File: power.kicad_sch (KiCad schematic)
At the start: 89 parts, among them Q1 PJE138K, Q2 PJE138K, Q3 SSM3J332R, Q4 PJE138K, Q5 SSM3J332R, Q6 PJE138K, Q7 SSM3J332R, U1 TLV70018_SC70, U4 TPS65150_HTSSOP, U5 MPQ7235GQBE, U6 TLV76701_WSON

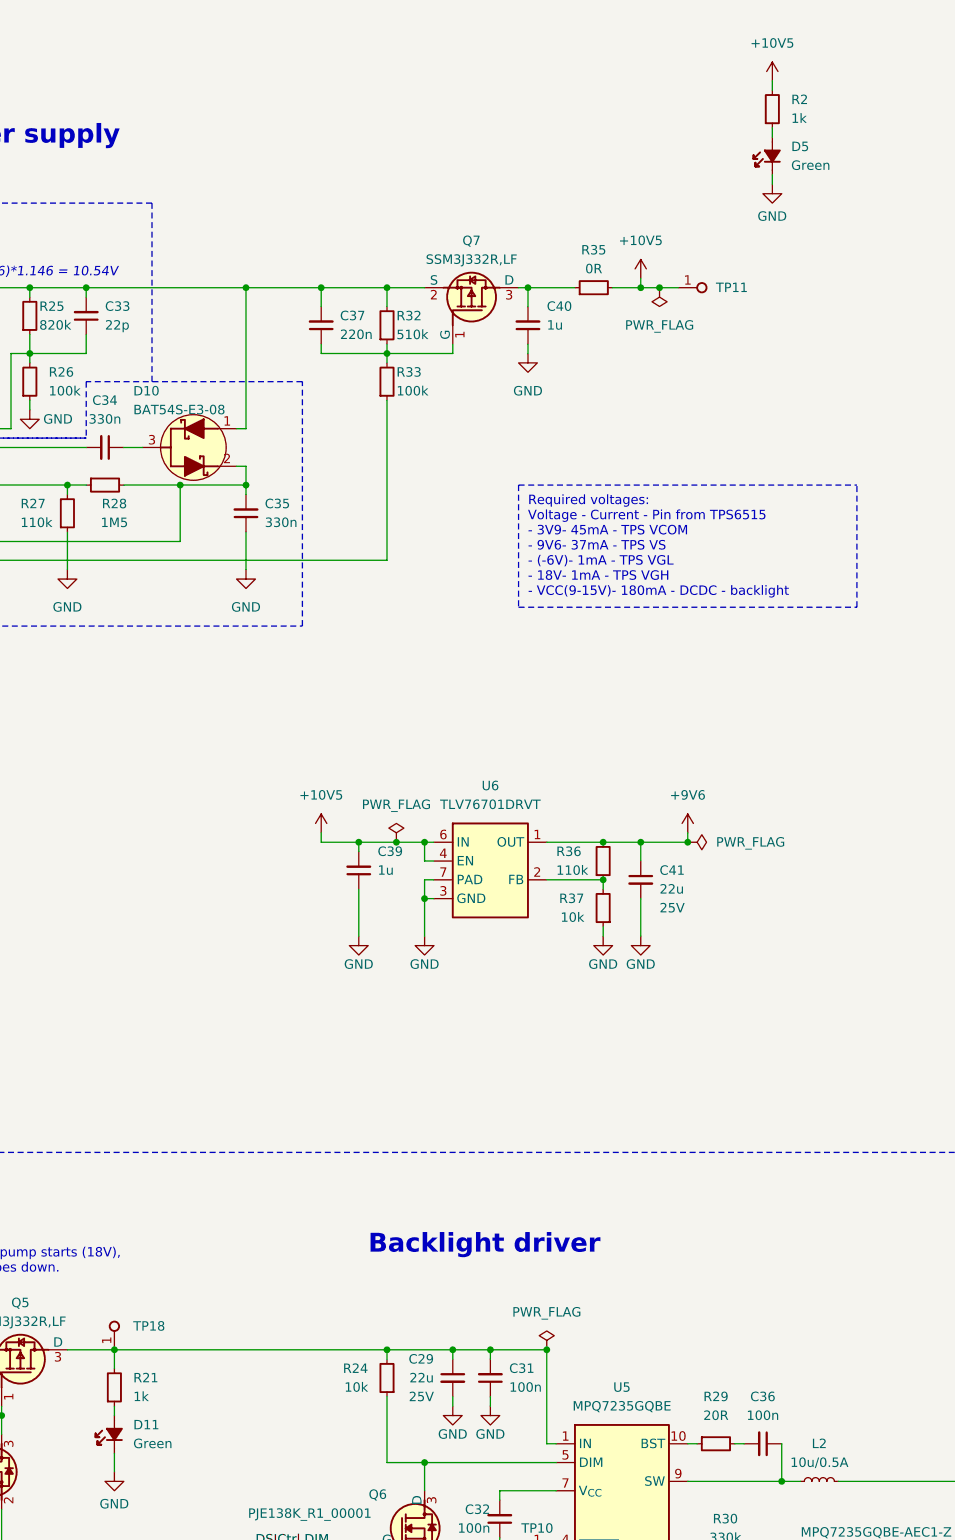
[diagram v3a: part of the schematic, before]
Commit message: [#73840] Update 3V3 LED resistors to 100R andd 10V5 LED resistors to 1k5
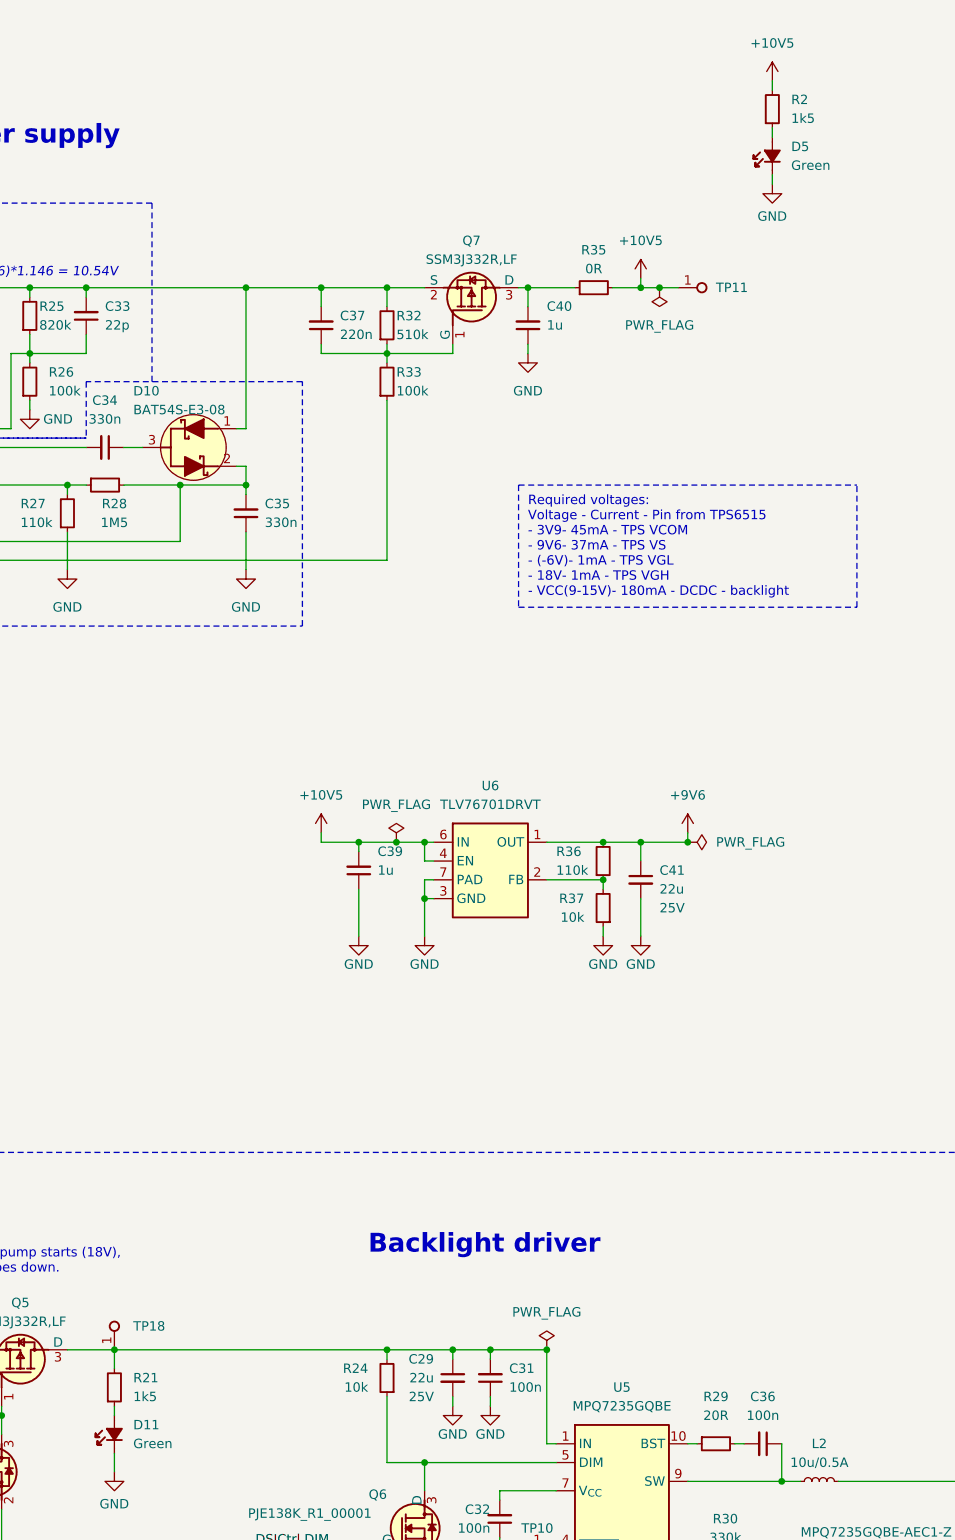
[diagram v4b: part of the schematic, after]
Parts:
- removed R2, R21: R_1k_0402, antmicro-footprints:R_0402_1005Metric, symbol antmicroResistors0402:R_1k_0402
- added R2, R21: R_1k5_0402, antmicro-footprints:R_0402_1005Metric, symbol antmicroResistors0402:R_1k5_0402
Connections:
- net +10V5: now also R2.2
- net at C29.1, C31.2, Q5.3 (D)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: now also R21.2
- net at D5.2 (A): now also R2.1
- net at D11.2 (A): now also R21.1
